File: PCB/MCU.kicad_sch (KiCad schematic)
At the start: 1 part, among them U1 STM32G491CETx

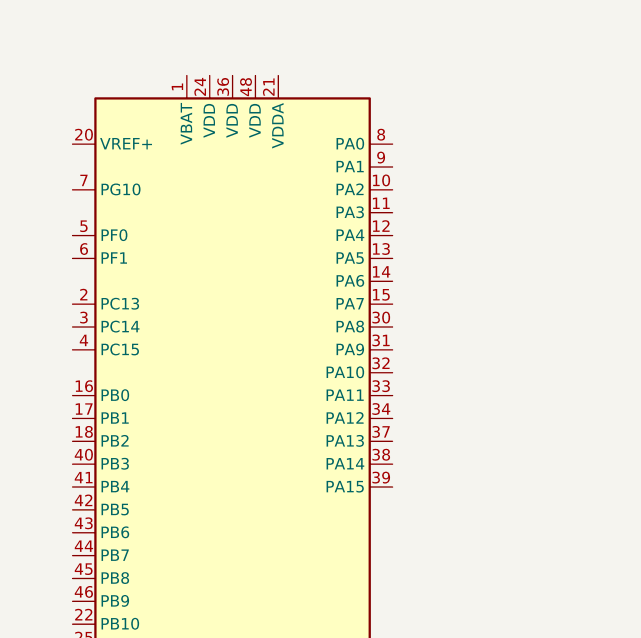
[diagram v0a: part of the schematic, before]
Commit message: switching to hall effect for now
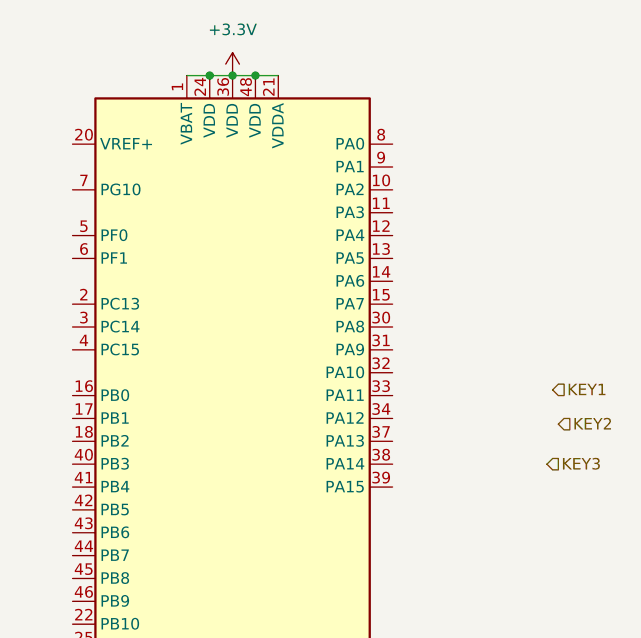
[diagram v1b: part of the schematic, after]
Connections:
- net +3.3V: now reaches U1.1 (VBAT)
- net +3.3V: now also U1.21 (VDDA), U1.24 (VDD), U1.36 (VDD), U1.48 (VDD)
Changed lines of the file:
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@@
+		)
+	)
+	(junction
+		(at 102.87 30.48)
+		(diameter 0)
+		(color 0 0 0 0)
+	)
+	(junction
+		(at 100.33 30.48)
+		(diameter 0)
+		(color 0 0 0 0)
+	)
+	(junction
+		(at 105.41 30.48)
+		(diameter 0)
+		(color 0 0 0 0)
+	)
+	(wire
+		(pts
+			(xy 100.33 30.48) (xy 102.87 30.48)
+		)
+		(stroke
+			(width 0)
+			(type default)
+		)
+	)
+	(wire
+		(pts
+			(xy 102.87 30.48) (xy 105.41 30.48)
+		)
+		(stroke
+			(width 0)
+			(type default)
+		)
+	)
+	(wire
+		(pts
+			(xy 97.79 30.48) (xy 100.33 30.48)
+		)
+		(stroke
+			(width 0)
+			(type default)
+		)
+	)
+	(wire
+		(pts
+			(xy 105.41 30.48) (xy 107.95 30.48)
+		)
+		(stroke
+			(width 0)
+			(type default)
+		)
+	)
+	(hierarchical_label "KEY2"
+		(shape input)
+		(at 139.065 69.215 0)
+		(effects
+			(font
+				(size 1.27 1.27)
+			)
+			(justify left)
+		)
+	)
+	(hierarchical_label "KEY1"
+		(shape input)
+		(at 138.43 65.405 0)
+		(effects
+			(font
+				(size 1.27 1.27)
+			)
+			(justify left)
+		)
+	)
+	(hierarchical_label "KEY3"
+		(shape input)
+		(at 137.795 73.66 0)
+		(effects
+			(font
+				(size 1.27 1.27)
+			)
+			(justify left)
 		)
 	)
@@
 					(unit 1)
 				)
+			)
+		)
+	)
+	(symbol
+		(lib_id "power:+3.3V")
+		(at 102.87 30.48 0)
+		(unit 1)
+		(exclude_from_sim no)
+		(in_bom yes)
+		(on_board yes)
+		(dnp no)
+		(fields_autoplaced yes)
+		(property "Reference" "#PWR011"
+			(at 102.87 34.29 0)
+			(effects
+				(font
+					(size 1.27 1.27)
+				)
+				(hide yes)
+			)
+		)
+		(property "Value" "+3.3V"
+			(at 102.87 25.4 0)
+			(effects
+				(font
+					(size 1.27 1.27)
+				)
+			)
+		)
+		(property "Footprint" ""
+			(at 102.87 30.48 0)
+			(effects
+				(font
+					(size 1.27 1.27)
+				)
+				(hide yes)
+			)
+		)
+		(property "Datasheet" ""
+			(at 102.87 30.48 0)
+			(effects
+				(font
+					(size 1.27 1.27)
+				)
+				(hide yes)
+			)
+		)
+		(property "Description" "Power symbol creates a global label with name \"+3.3V\""
+			(at 102.87 30.48 0)
+			(effects
+				(font
+					(size 1.27 1.27)
+				)
+				(hide yes)
+			)
+		)
+		(pin "1"
+		)
+		(instances
+			(project ""
+				(path "/f410b0a0-725c-464e-80be-c0074224226d/14486a70-ff57-4274-bd42-24831c317bcd"
+					(reference "#PWR011")
+					(unit 1)
+				)

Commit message: cramming for portfolio
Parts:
- added C1, C2: C, Capacitor_SMD:C_0603_1608Metric_Pad1.08x0.95mm_HandSolder, symbol Device:C
- added C3: 0.1uF, Capacitor_SMD:C_0603_1608Metric_Pad1.08x0.95mm_HandSolder, symbol Device:C
- added R1: 10k, Resistor_SMD:R_0603_1608Metric_Pad0.98x0.95mm_HandSolder, symbol Device:R_US
- added Reset1: Reset, TL3365AF180QG:TL3365AF180QG, symbol Switch:SW_Push
- added SW1: SW_SPDT, UTSVT_Special:SW_CJS-1200TA, symbol Switch:SW_SPDT
- added Y1: Crystal, Crystal:Crystal_SMD_Abracon_ABM3-2Pin_5.0x3.2mm, symbol Device:Crystal
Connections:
- net KEY1: now also U1.27 (PB13)
- net KEY2: now also U1.28 (PB14)
- net KEY3: now also U1.29 (PB15)
- net DC: now reaches U1.10 (PA2)
- net CS: now reaches U1.11 (PA3)
- net BL: now reaches U1.12 (PA4)
- net SCK: now reaches U1.13 (PA5)
- net MISO: now reaches U1.14 (PA6)
- net MOSI: now reaches U1.15 (PA7)
- net GND: now reaches U1.19 (VSSA)
- net GND: now also U1.23 (VSS), U1.35 (VSS), U1.47 (VSS), C1.2, C2.1, C3.2, Reset1.2, SW1.3 (C)
- net AddressableLEDs: now reaches U1.25 (PB11)
- net USB_D-: now reaches U1.33 (PA11)
- net USB_D+: now reaches U1.34 (PA12)
- net BOOT: now reaches U1.45 (PB8)
- net BOOT: now also SW1.2 (B)
- net at U1.5 (PF0): now also C1.1, Y1.1
- net at U1.6 (PF1): now also C2.2, Y1.2
- net NRST: now reaches U1.7 (PG10)
- net NRST: now also C3.1, R1.1, Reset1.1
- net RES: now reaches U1.9 (PA1)
- new net +3V3: R1.2, SW1.1 (A)
- no-connect marks 0 -> 23
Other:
- note added: "Boot Switch"
- note added: "Reset Button"

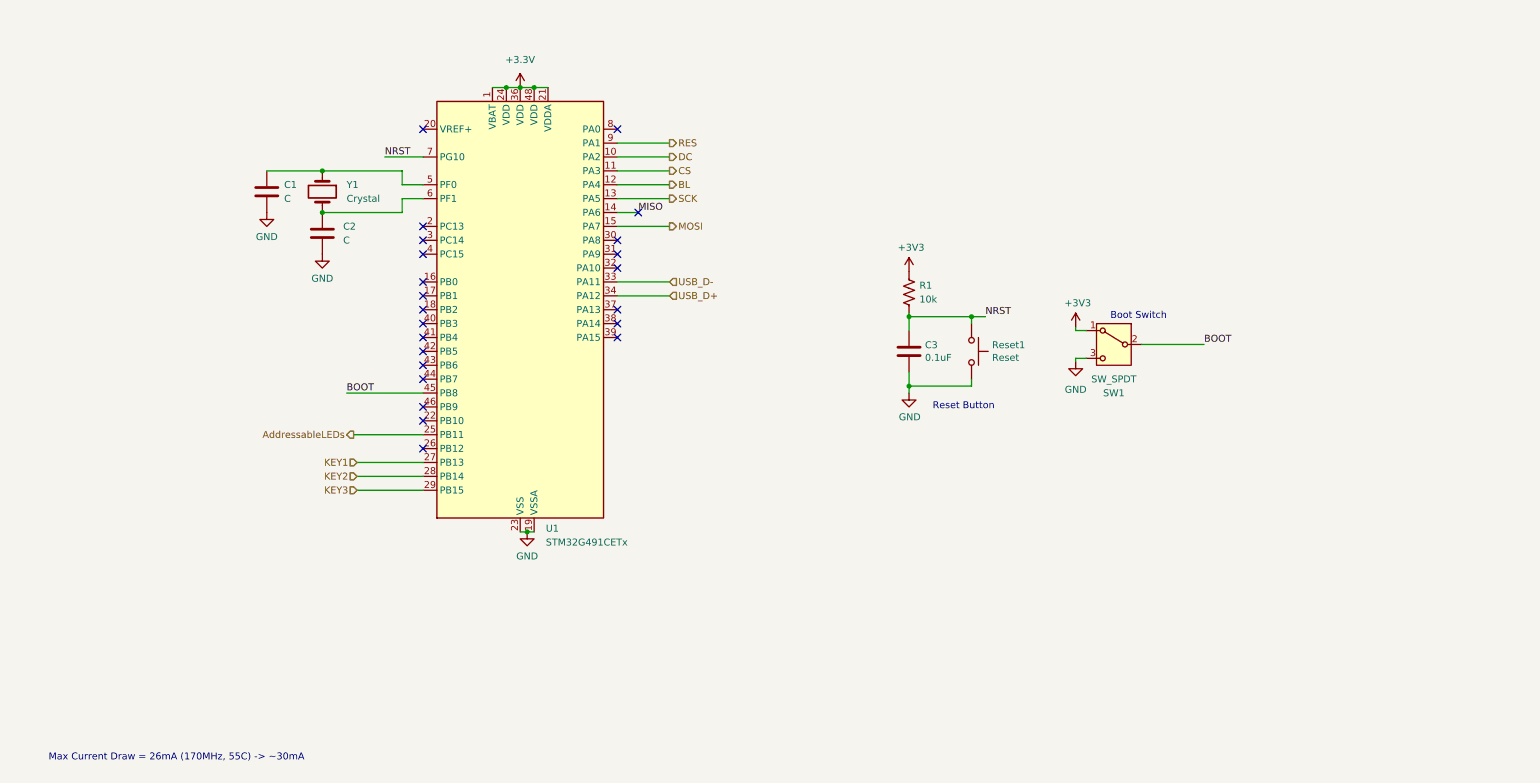
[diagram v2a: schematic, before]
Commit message: only need to find boot and reset footprints
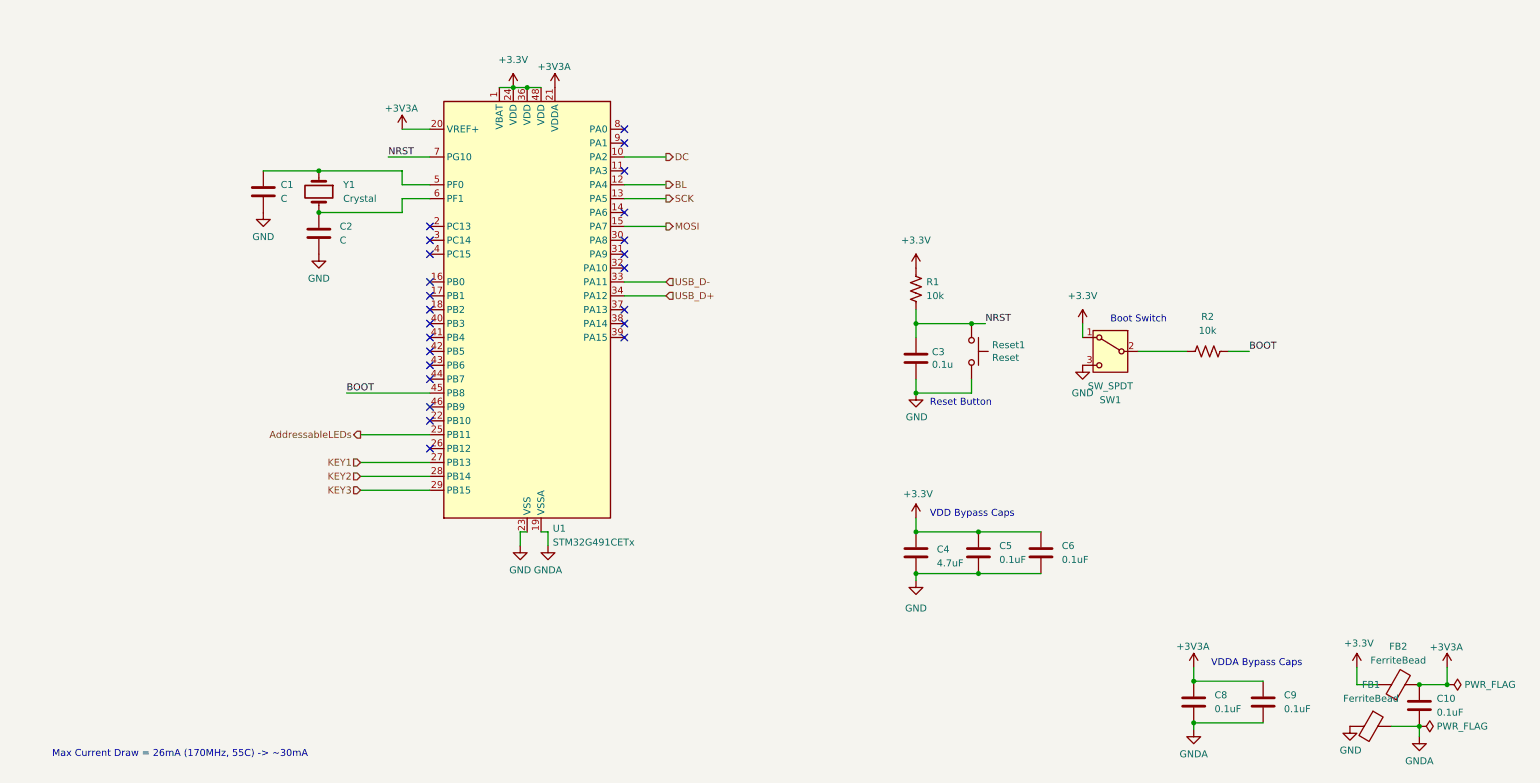
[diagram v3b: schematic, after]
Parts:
- added C10, C5, C6, C8, C9: 0.1uF, Capacitor_SMD:C_0603_1608Metric_Pad1.08x0.95mm_HandSolder, symbol Device:C
- added C4: 4.7uF, Capacitor_SMD:C_0805_2012Metric, symbol Device:C
- added FB1, FB2: FerriteBead, Inductor_SMD:L_0603_1608Metric_Pad1.05x0.95mm_HandSolder, symbol Device:FerriteBead
- added R2: 10k, Resistor_SMD:R_0603_1608Metric_Pad0.98x0.95mm_HandSolder, symbol Device:R_US
- C3: value 0.1uF -> 0.1u
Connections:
- net +3V3 is gone; now on net +3.3V: R1.2, SW1.1 (A)
- net +3.3V: now also C4.1, C5.1, C6.1, FB2.1; no longer U1.21 (VDDA)
- net BOOT: now also R2.1; no longer SW1.2 (B)
- net GND: now also C4.2, C5.2, C6.2, FB1.2; no longer U1.19 (VSSA)
- net +3V3A: now reaches U1.20 (VREF+)
- net +3V3A: now also U1.21 (VDDA), C10.1, C8.1, C9.1, FB2.2
- net CS: no longer names the net of U1.11 (PA3)
- net MISO: no longer names the net of U1.14 (PA6)
- net RES: no longer names the net of U1.9 (PA1)
- new net: R2.2, SW1.2 (B)
- new net GNDA: C10.2, C8.2, C9.2, FB1.1, U1.19 (VSSA)
- no-connect marks 23 -> 24
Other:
- note added: "VDD Bypass Caps"
- note added: "VDDA Bypass Caps"
- moved on the sheet: C1, C2, C3, R1, SW1, U1, Y1

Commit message: testing out g431
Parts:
- removed U1: STM32G491CETx, Package_QFP:LQFP-48_7x7mm_P0.5mm, symbol MCU_ST_STM32G4:STM32G491CETx
- added U9: STM32G431CBTx, Package_QFP:LQFP-48_7x7mm_P0.5mm, symbol MCU_ST_STM32G4:STM32G431CBTx
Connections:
- net +3.3V: now also U9.1 (VBAT), U9.24 (VDD), U9.36 (VDD), U9.48 (VDD)
- net +3V3A: now also U9.20 (VREF+), U9.21 (VDDA)
- net AddressableLEDs: now also U9.25 (PB11)
- net BL: now also U9.12 (PA4)
- net BOOT: now also U9.45 (PB8)
- net DC: now also U9.10 (PA2)
- net GND: now also U9.23 (VSS), U9.35 (VSS), U9.47 (VSS)
- net GNDA: now also U9.19 (VSSA)
- net KEY1: now also U9.27 (PB13)
- net KEY2: now also U9.28 (PB14)
- net KEY3: now also U9.29 (PB15)
- net MOSI: now also U9.15 (PA7)
- net NRST: now also U9.7 (PG10)
- net SCK: now also U9.13 (PA5)
- net USB_D+: now also U9.34 (PA12)
- net USB_D-: now also U9.33 (PA11)
- net at C1.1, Y1.1: now also U9.5 (PF0)
- net at C2.2, Y1.2: now also U9.6 (PF1)
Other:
- moved on the sheet: C10, C8, C9, FB1, FB2

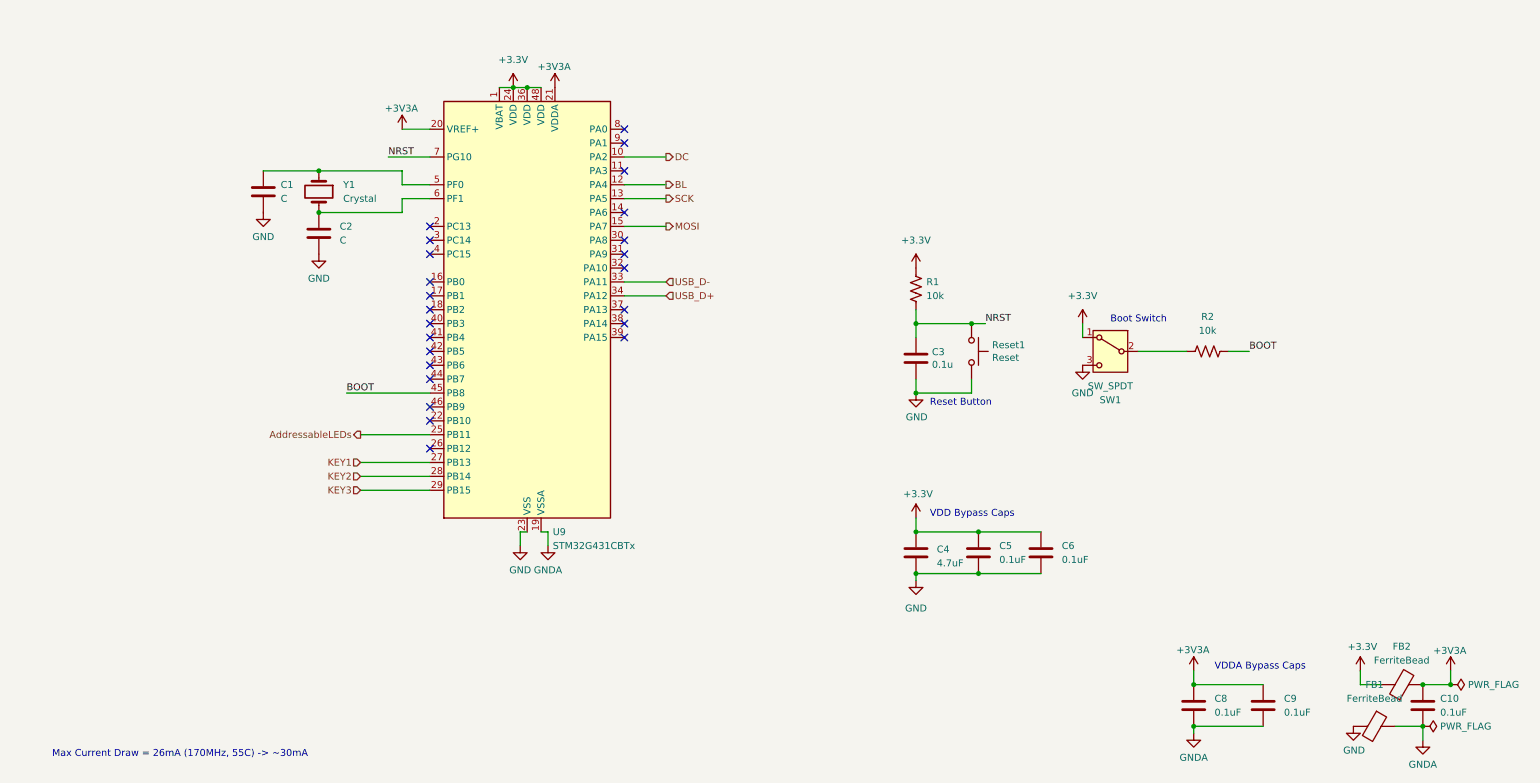
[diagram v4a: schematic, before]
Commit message: changing to wasd
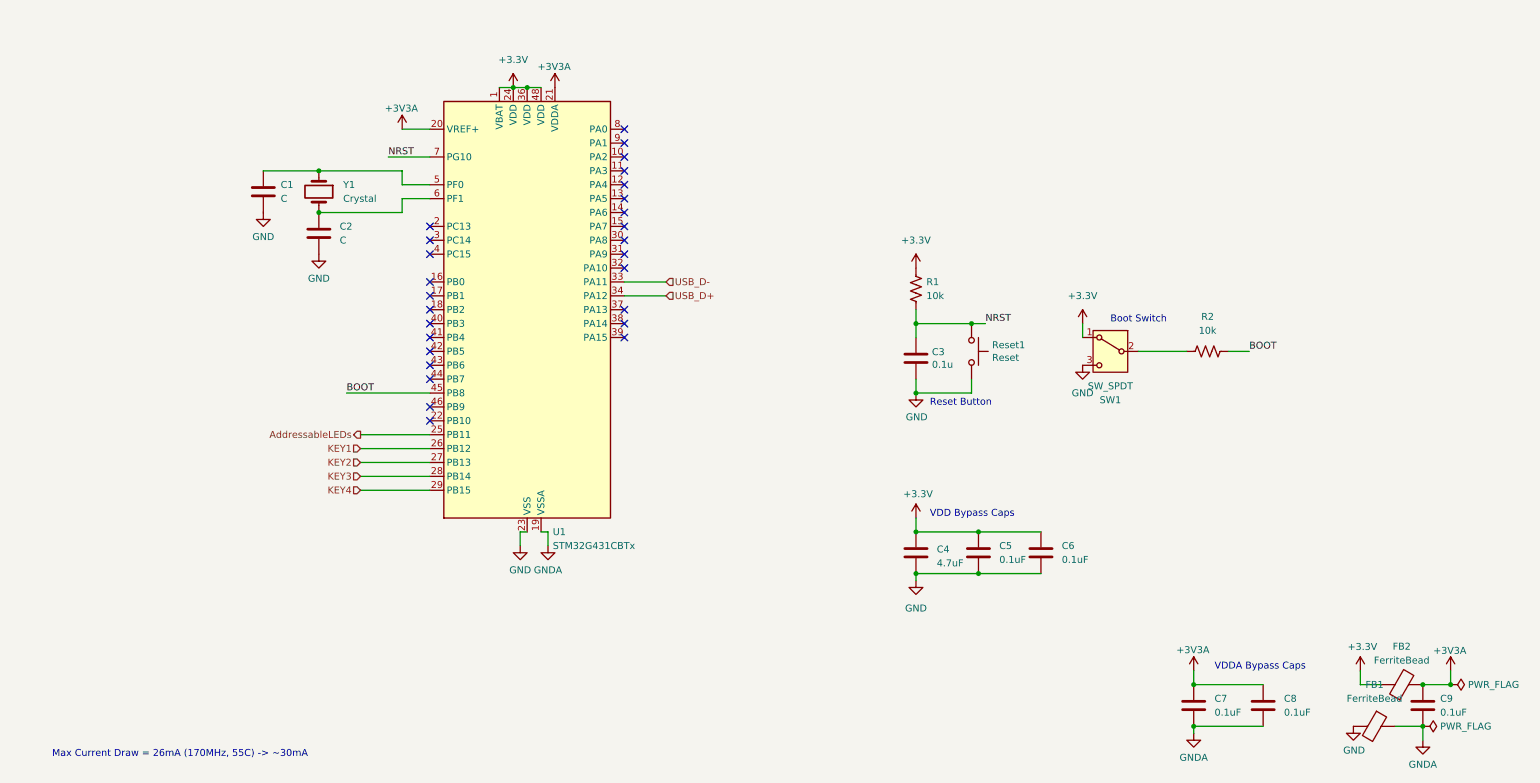
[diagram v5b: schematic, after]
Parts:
- renumbered C8 to C7, C9 to C8, C10 to C9, U9 to U1
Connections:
- net KEY1: now also U1.26 (PB12); no longer U1.27 (PB13)
- net KEY2: now also U1.27 (PB13); no longer U1.28 (PB14)
- net KEY3: now also U1.28 (PB14); no longer U1.29 (PB15)
- net BL: no longer names the net of U1.12 (PA4)
- net DC: no longer names the net of U1.10 (PA2)
- net MOSI: no longer names the net of U1.15 (PA7)
- net SCK: no longer names the net of U1.13 (PA5)
- new net KEY4: U1.29 (PB15)
- no-connect marks 24 -> 27
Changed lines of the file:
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@@
 	)
 	(no_connect
+		(at 121.92 43.18)
+	)
+	(no_connect
+		(at 121.92 50.8)
+	)
+	(no_connect
 		(at 86.36 58.42)
 	)
 	(no_connect
-		(at 121.92 73.66)
+		(at 121.92 48.26)
 	)
 	(no_connect
-		(at 86.36 96.52)
+		(at 121.92 73.66)
 	)
 	(no_connect
@@
 	)
 	(no_connect
+		(at 121.92 55.88)
+	)
+	(no_connect
 		(at 86.36 76.2)
 	)
@@
 	(wire
 		(pts
-			(xy 102.87 111.76) (xy 104.14 111.76)
+			(xy 73.66 96.52) (xy 86.36 96.52)
 		)
 		(stroke
@@
 	(wire
 		(pts
-			(xy 226.06 147.32) (xy 238.76 147.32)
+			(xy 102.87 111.76) (xy 104.14 111.76)
 		)
 		(stroke
@@
 	(wire
 		(pts
-			(xy 256.54 137.16) (xy 256.54 139.7)
+			(xy 226.06 147.32) (xy 238.76 147.32)
 		)
 		(stroke
@@
 	(wire
 		(pts
-			(xy 121.92 55.88) (xy 129.54 55.88)
+			(xy 256.54 137.16) (xy 256.54 139.7)
 		)
 		(stroke
@@
 	(wire
 		(pts
-			(xy 121.92 43.18) (xy 129.54 43.18)
-		)
-		(stroke
-			(width 0)
-			(type default)
-		)
-	)
-	(wire
-		(pts
 			(xy 185.42 73.66) (xy 187.96 73.66)
 		)
@@
 	(wire
 		(pts
-			(xy 129.54 50.8) (xy 121.92 50.8)
-		)
-		(stroke
-			(width 0)
-			(type default)
-		)
-	)
-	(wire
-		(pts
 			(xy 205.74 76.2) (xy 205.74 73.66)
 		)
@@
 	(wire
 		(pts
-			(xy 121.92 48.26) (xy 129.54 48.26)
-		)
-		(stroke
-			(width 0)
-			(type default)
-		)
-	)
-	(wire
-		(pts
 			(xy 73.66 99.06) (xy 86.36 99.06)
 		)
@@
 		)
 	)
-	(hierarchical_label "KEY2"
+	(hierarchical_label "KEY4"
 		(shape input)
-		(at 73.66 101.6 180)
+		(at 73.66 104.14 180)
 		(effects
 			(font
@@
 		)
 	)
-	(hierarchical_label "KEY1"
+	(hierarchical_label "KEY2"
 		(shape input)
 		(at 73.66 99.06 180)
@@
 		)
 	)
-	(hierarchical_label "KEY3"
-		(shape input)
-		(at 73.66 104.14 180)
-		(effects
-			(font
-				(size 1.27 1.27)
-			)
-			(justify right)
-		)
-	)
-	(hierarchical_label "DC"
-		(shape output)
-		(at 129.54 43.18 0)
-		(effects
-			(font
-				(size 1.27 1.27)
-			)
-			(justify left)
-		)
-	)
 	(hierarchical_label "USB_D+"
 		(shape input)
@@
 		)
 	)
-	(hierarchical_label "MOSI"
-		(shape output)
-		(at 129.54 55.88 0)
+	(hierarchical_label "KEY3"
+		(shape input)
+		(at 73.66 101.6 180)
 		(effects
 			(font
 				(size 1.27 1.27)
 			)
-			(justify left)
+			(justify right)
 		)
 	)
-	(hierarchical_label "BL"
-		(shape output)
-		(at 129.54 48.26 0)
+	(hierarchical_label "KEY1"
+		(shape input)
+		(at 73.66 96.52 180)
 		(effects
 			(font
 				(size 1.27 1.27)
 			)
-			(justify left)
+			(justify right)
 		)
 	)
@@
 		)
 	)
-	(hierarchical_label "SCK"
-		(shape output)
-		(at 129.54 50.8 0)
-		(effects
-			(font
-				(size 1.27 1.27)
-			)
-			(justify left)
-		)
-	)
 	(symbol
 		(lib_id "power:+3.3V")
@@
 		(dnp no)
 		(fields_autoplaced yes)
-		(property "Reference" "C9"
+		(property "Reference" "C8"
 			(at 242.57 142.2399 0)
 			(effects
@@
 			(project "OTCboard"
 				(path "/f410b0a0-725c-464e-80be-c0074224226d/14486a70-ff57-4274-bd42-24831c317bcd"
-					(reference "C9")
+					(reference "C8")
 					(unit 1)
 				)
@@
 		(dnp no)
 		(fields_autoplaced yes)
-		(property "Reference" "C8"
+		(property "Reference" "C7"
 			(at 229.87 142.2399 0)
 			(effects
@@
 			(project "OTCboard"
 				(path "/f410b0a0-725c-464e-80be-c0074224226d/14486a70-ff57-4274-bd42-24831c317bcd"
-					(reference "C8")
+					(reference "C7")
 					(unit 1)
 				)
@@
 		(dnp no)
 		(fields_autoplaced yes)
-		(property "Reference" "C10"
+		(property "Reference" "C9"
 			(at 271.145 142.2399 0)
 			(effects
@@
 			(project "OTCboard"
 				(path "/f410b0a0-725c-464e-80be-c0074224226d/14486a70-ff57-4274-bd42-24831c317bcd"
-					(reference "C10")
+					(reference "C9")
 					(unit 1)
 				)
@@
 		(dnp no)
 		(fields_autoplaced yes)
-		(property "Reference" "U9"
+		(property "Reference" "U1"
 			(at 108.8233 111.76 0)
 			(effects
@@
 			(project ""
 				(path "/f410b0a0-725c-464e-80be-c0074224226d/14486a70-ff57-4274-bd42-24831c317bcd"
-					(reference "U9")
+					(reference "U1")
 					(unit 1)
 				)

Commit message: new update
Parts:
- C1, C2: value C -> 26p
- C4: footprint Capacitor_SMD:C_0805_2012Metric -> Capacitor_SMD:C_0805_2012Metric_Pad1.18x1.45mm_HandSolder
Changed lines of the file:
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@@
 			)
 		)
-		(property "Value" "C"
+		(property "Value" "26p"
 			(at 69.85 58.4199 0)
 			(effects
@@
 			)
 		)
-		(property "Footprint" "Capacitor_SMD:C_0805_2012Metric"
+		(property "Footprint" "Capacitor_SMD:C_0805_2012Metric_Pad1.18x1.45mm_HandSolder"
 			(at 176.2252 119.38 0)
 			(effects
@@
 		(fields_autoplaced yes)
 		(property "Reference" "C1"
-			(at 59.055 48.2599 0)
+			(at 59.69 48.2599 0)
 			(effects
 				(font
@@
 			)
 		)
-		(property "Value" "C"
-			(at 59.055 50.7999 0)
-			(effects
-				(font
+		(property "Value" "26p"
+			(at 59.69 50.7999 0)
+			(effects
+				(font
